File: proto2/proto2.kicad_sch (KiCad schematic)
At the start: 10 parts, among them J13 Daughter Card, SW1 SW_DIP_x04

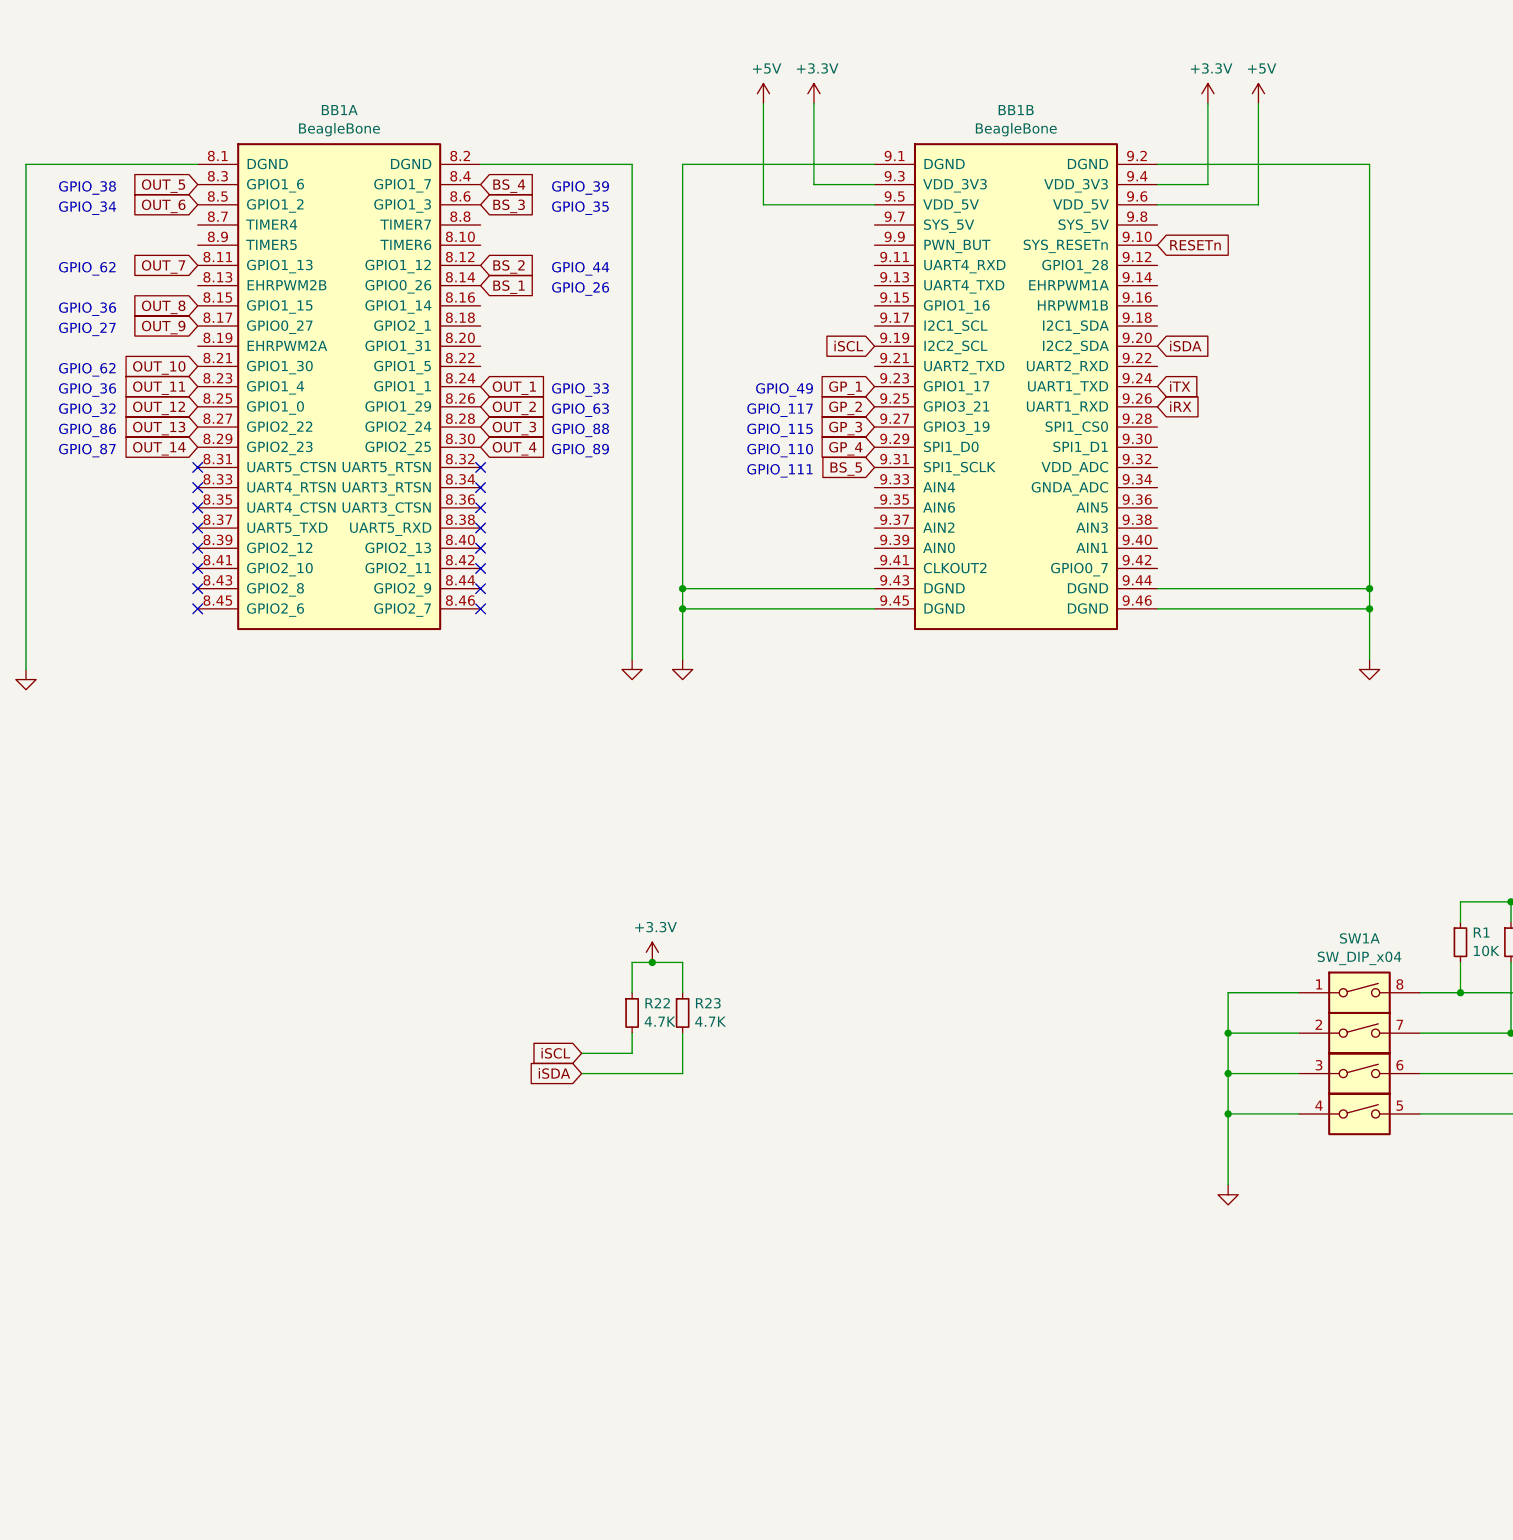
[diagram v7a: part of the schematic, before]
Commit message: Rerouting outputs, adding integrated analog input.
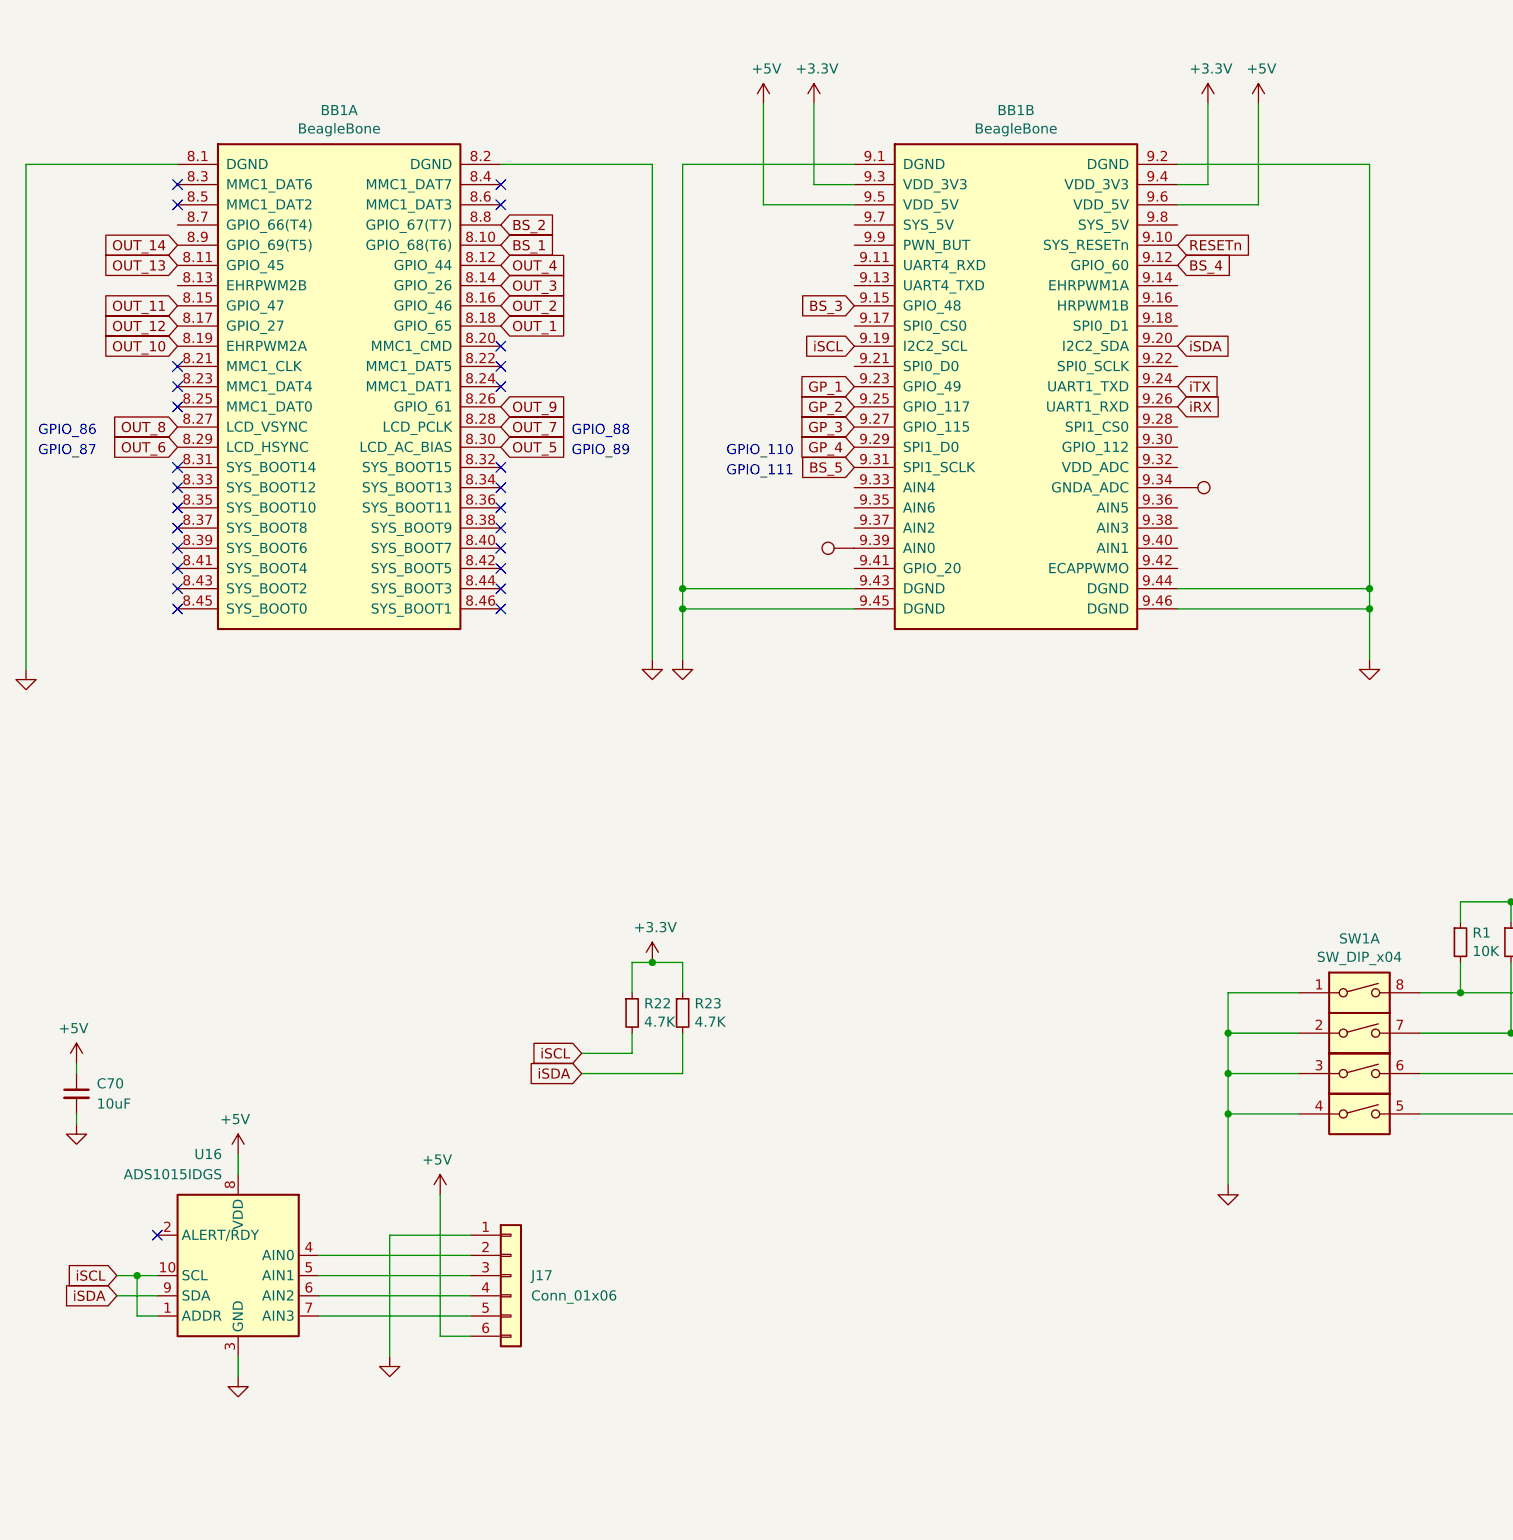
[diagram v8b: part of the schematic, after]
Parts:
- added C70: 10uF, Capacitor_SMD:C_0805_2012Metric, symbol Device:C_Small
- added J17: Conn_01x06, Connector_BCR:Phoenix_Contact_PST_6, symbol Connector_Generic:Conn_01x06
- added TP66, TP67: TestPoint, symbol Connector:TestPoint
- added U16: ADS1015IDGS, Package_SO:TSSOP-10_3x3mm_P0.5mm, symbol Analog_ADC:ADS1015IDGS
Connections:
- net +5V: now also C70.1, J17.6 (Pin_6), U16.8 (VDD)
- net BS_1: now also BB1.8.10 (GPIO_68(T6)); no longer BB1.8.14 (GPIO0_26)
- net BS_2: now also BB1.8.8 (GPIO_67(T7)); no longer BB1.8.12 (GPIO1_12)
- net BS_3: now also BB1.9.15 (GPIO_48); no longer BB1.8.6 (GPIO1_3)
- net BS_4: now also BB1.9.12 (GPIO_60); no longer BB1.8.4 (GPIO1_7)
- net GND-SIG: now also C70.2, J17.1 (Pin_1), U16.3 (GND)
- net OUT_1: now also BB1.8.18 (GPIO_65); no longer BB1.8.24 (GPIO1_1)
- net OUT_10: now also BB1.8.19 (EHRPWM2A); no longer BB1.8.21 (GPIO1_30)
- net OUT_11: now also BB1.8.15 (GPIO_47); no longer BB1.8.23 (GPIO1_4)
- net OUT_12: now also BB1.8.17 (GPIO_27); no longer BB1.8.25 (GPIO1_0)
- net OUT_13: now also BB1.8.11 (GPIO_45); no longer BB1.8.27 (GPIO2_22)
- net OUT_14: now also BB1.8.9 (GPIO_69(T5)); no longer BB1.8.29 (GPIO2_23)
- net OUT_2: now also BB1.8.16 (GPIO_46); no longer BB1.8.26 (GPIO1_29)
- net OUT_3: now also BB1.8.14 (GPIO_26); no longer BB1.8.28 (GPIO2_24)
- net OUT_4: now also BB1.8.12 (GPIO_44); no longer BB1.8.30 (GPIO2_25)
- net OUT_5: now also BB1.8.30 (LCD_AC_BIAS); no longer BB1.8.3 (GPIO1_6)
- net OUT_6: now also BB1.8.29 (LCD_HSYNC); no longer BB1.8.5 (GPIO1_2)
- net OUT_7: now also BB1.8.28 (LCD_PCLK); no longer BB1.8.11 (GPIO1_13)
- net OUT_8: now also BB1.8.27 (LCD_VSYNC); no longer BB1.8.15 (GPIO1_15)
- net OUT_9: now also BB1.8.26 (GPIO_61); no longer BB1.8.17 (GPIO0_27)
- net iSCL: now also U16.1 (ADDR), U16.10 (SCL)
- net iSDA: now also U16.9 (SDA)
- net at BB1.9.34 (GNDA_ADC): now also TP67.1
- net at BB1.9.39 (AIN0): now also TP66.1
- new net: J17.2 (Pin_2), U16.4 (AIN0)
- new net: J17.3 (Pin_3), U16.5 (AIN1)
- new net: J17.4 (Pin_4), U16.6 (AIN2)
- new net: J17.5 (Pin_5), U16.7 (AIN3)
- no-connect marks 16 -> 27
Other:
- note removed: "GPIO_115"
- note removed: "GPIO_117"
- note removed: "GPIO_26"
- note removed: "GPIO_27"
- note removed: "GPIO_32"
- note removed: "GPIO_33"
- note removed: "GPIO_34"
- note removed: "GPIO_35"
- note removed: "GPIO_36"
- note removed: "GPIO_38"
- note removed: "GPIO_39"
- note removed: "GPIO_44"
- note removed: "GPIO_49"
- note removed: "GPIO_62"
- note removed: "GPIO_63"
